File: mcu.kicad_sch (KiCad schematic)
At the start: 30 parts, among them J1 SM03B-SRSS-TB, SW1 SW_Push, SW2 SW_Push, U1 RP2350_60QFN, U2 W25Q128JVS, Y1 ABM8-272-T3

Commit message: minor cleanup
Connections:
- net GND: no longer J1.MP (MountPin)
- no-connect marks 8 -> 9
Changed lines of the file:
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@@
-	)
-	(junction
-		(at 242.57 138.43)
-		(diameter 0)
-		(color 0 0 0 0)
 	)
 	(junction
@@
 	)
 	(no_connect
+		(at 248.92 137.16)
+	)
+	(no_connect
 		(at 175.26 147.32)
 	)
@@
 	(wire
 		(pts
-			(xy 242.57 138.43) (xy 242.57 140.97)
+			(xy 242.57 129.54) (xy 242.57 140.97)
 		)
 		(stroke
@@
 	(wire
 		(pts
-			(xy 242.57 138.43) (xy 248.92 138.43)
-		)
-		(stroke
-			(width 0)
-			(type default)
-		)
-	)
-	(wire
-		(pts
 			(xy 175.26 68.58) (xy 185.42 68.58)
 		)
@@
 	(wire
 		(pts
-			(xy 242.57 129.54) (xy 242.57 138.43)
-		)
-		(stroke
-			(width 0)
-			(type default)
-		)
-	)
-	(wire
-		(pts
 			(xy 201.93 41.91) (xy 190.5 41.91)
 		)
@@
 		)
 		(stroke
-			(width 0)
-			(type default)
-		)
-	)
-	(wire
-		(pts
-			(xy 248.92 137.16) (xy 248.92 138.43)
-		)
-		(stroke

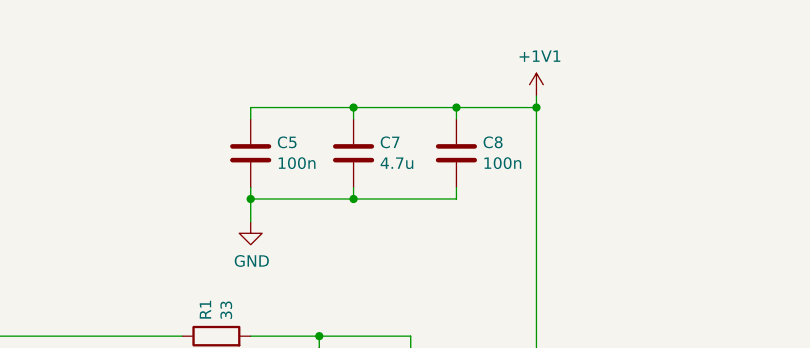
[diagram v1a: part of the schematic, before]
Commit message: add silkscreen, optimize layout and replace sd card peripheral
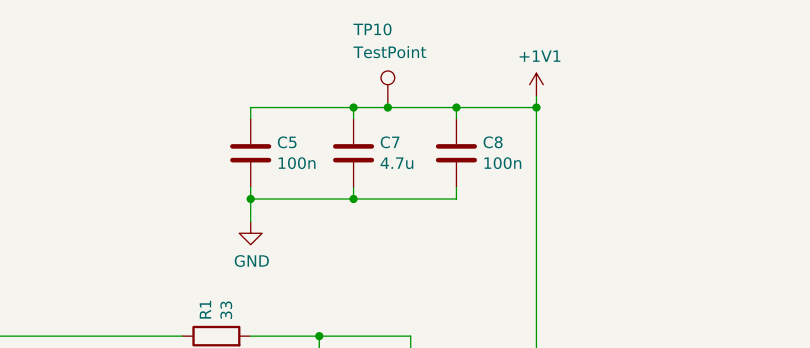
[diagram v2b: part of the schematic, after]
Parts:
- added TP10: TestPoint, TestPoint:TestPoint_Pad_D1.0mm, symbol Connector:TestPoint
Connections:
- net +1V1: now also TP10.1
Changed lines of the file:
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@@
+	)
+	(junction
+		(at 104.14 30.48)
+		(diameter 0)
+		(color 0 0 0 0)
 	)
 	(junction
@@
 	(wire
 		(pts
+			(xy 104.14 30.48) (xy 111.76 30.48)
+		)
+		(stroke
+			(width 0)
+			(type default)
+		)
+	)
+	(wire
+		(pts
 			(xy 62.23 82.55) (xy 111.76 82.55)
 		)
@@
 	(wire
 		(pts
-			(xy 100.33 30.48) (xy 111.76 30.48)
+			(xy 100.33 30.48) (xy 104.14 30.48)
 		)
 		(stroke
@@
 					(unit 1)
 				)
+			)
+		)
+	)
+	(symbol
+		(lib_id "Connector:TestPoint")
+		(at 104.14 30.48 0)
+		(unit 1)
+		(exclude_from_sim no)
+		(in_bom yes)
+		(on_board yes)
+		(dnp no)
+		(property "Reference" "TP10"
+			(at 100.33 21.844 0)
+			(effects
+				(font
+					(size 1.27 1.27)
+				)
+				(justify left)
+			)
+		)
+		(property "Value" "TestPoint"
+			(at 100.33 24.384 0)
+			(effects
+				(font
+					(size 1.27 1.27)
+				)
+				(justify left)
+			)
+		)
+		(property "Footprint" "TestPoint:TestPoint_Pad_D1.0mm"
+			(at 109.22 30.48 0)
+			(effects
+				(font
+					(size 1.27 1.27)
+				)
+				(hide yes)
+			)
+		)
+		(property "Datasheet" "~"
+			(at 109.22 30.48 0)
+			(effects
+				(font
+					(size 1.27 1.27)
+				)
+				(hide yes)
+			)
+		)
+		(property "Description" "test point"
+			(at 104.14 30.48 0)
+			(effects
+				(font
+					(size 1.27 1.27)
+				)
+				(hide yes)
+			)
+		)
+		(property "LCSC" ""
+			(at 104.14 30.48 0)
+			(effects
+				(font
+					(size 1.27 1.27)
+				)
+				(hide yes)
+			)
+		)
+		(property "Manufacturer" ""
+			(at 104.14 30.48 0)
+			(effects
+				(font
+					(size 1.27 1.27)
+				)
+				(hide yes)
+			)
+		)
+		(property "Manufacturer Part Number" ""
+			(at 104.14 30.48 0)
+			(effects
+				(font
+					(size 1.27 1.27)
+				)
+				(hide yes)
+			)
+		)
+		(pin "1"
+		)
+		(instances
+			(project "gameboy"
+				(path "/f4643692-c319-40a7-82a2-3e775c0a417f/0c43a605-cda2-4793-9a29-301f6419db25"
+					(reference "TP10")
+					(unit 1)
+				)

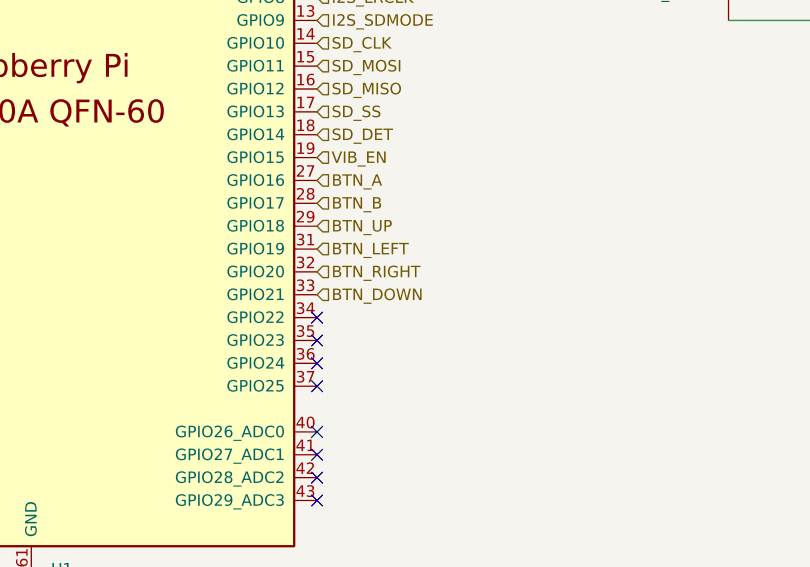
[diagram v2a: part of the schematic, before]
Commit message: add power monitoring
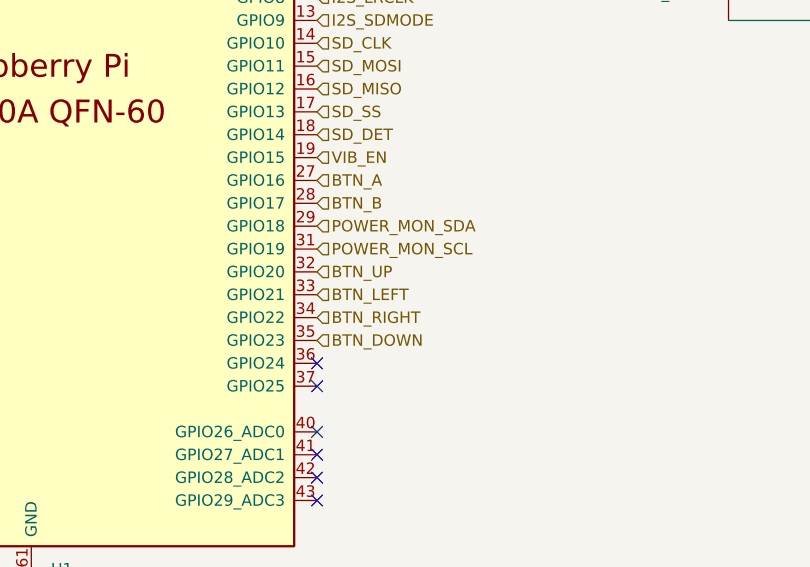
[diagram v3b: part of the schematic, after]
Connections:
- net BTN_DOWN: now also U1.35 (GPIO23); no longer U1.33 (GPIO21)
- net BTN_LEFT: now also U1.33 (GPIO21); no longer U1.31 (GPIO19)
- net BTN_RIGHT: now also U1.34 (GPIO22); no longer U1.32 (GPIO20)
- net BTN_UP: now also U1.32 (GPIO20); no longer U1.29 (GPIO18)
- new net POWER_MON_SCL: U1.31 (GPIO19)
- new net POWER_MON_SDA: U1.29 (GPIO18)
- no-connect marks 9 -> 7
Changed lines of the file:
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@@
-	)
-	(no_connect
-		(at 175.26 137.16)
 	)
 	(no_connect
@@
 	)
 	(no_connect
-		(at 175.26 134.62)
-	)
-	(no_connect
 		(at 248.92 137.16)
 	)
@@
 	(hierarchical_label "BTN_UP"
 		(shape input)
+		(at 175.26 129.54 0)
+		(effects
+			(font
+				(size 1.27 1.27)
+			)
+			(justify left)
+		)
+	)
+	(hierarchical_label "SD_MISO"
+		(shape input)
+		(at 175.26 109.22 0)
+		(effects
+			(font
+				(size 1.27 1.27)
+			)
+			(justify left)
+		)
+	)
+	(hierarchical_label "SD_MOSI"
+		(shape input)
+		(at 175.26 106.68 0)
+		(effects
+			(font
+				(size 1.27 1.27)
+			)
+			(justify left)
+		)
+	)
+	(hierarchical_label "POWER_MON_SDA"
+		(shape input)
 		(at 175.26 124.46 0)
 		(effects
@@
 		)
 	)
-	(hierarchical_label "SD_MISO"
-		(shape input)
-		(at 175.26 109.22 0)
-		(effects
-			(font
-				(size 1.27 1.27)
-			)
-			(justify left)
-		)
-	)
-	(hierarchical_label "SD_MOSI"
-		(shape input)
-		(at 175.26 106.68 0)
-		(effects
-			(font
-				(size 1.27 1.27)
-			)
-			(justify left)
-		)
-	)
 	(hierarchical_label "LCD_DC"
 		(shape input)
@@
 		)
 	)
+	(hierarchical_label "POWER_MON_SCL"
+		(shape input)
+		(at 175.26 127 0)
+		(effects
+			(font
+				(size 1.27 1.27)
+			)
+			(justify left)
+		)
+	)
 	(hierarchical_label "I2S_DIN"
 		(shape input)
@@
 	(hierarchical_label "BTN_RIGHT"
 		(shape input)
-		(at 175.26 129.54 0)
+		(at 175.26 134.62 0)
 		(effects
 			(font
@@
 	(hierarchical_label "BTN_LEFT"
 		(shape input)
-		(at 175.26 127 0)
+		(at 175.26 132.08 0)
 		(effects
 			(font
@@
 	(hierarchical_label "BTN_DOWN"
 		(shape input)
-		(at 175.26 132.08 0)
-		(effects
-			(font
+		(at 175.26 137.16 0)
+		(effects
+			(font

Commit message: changes for production
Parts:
- R2, R3, R6: footprint Resistor_SMD:R_0402_1005Metric -> Resistor_SMD:R_0603_1608Metric
- SW1, SW2: LCSC (none) -> C5504987; Manufacturer (none) -> Wurth Elektronik; Manufacturer Part Number (none) -> 434133025816
- TP10: now left out of the parts list
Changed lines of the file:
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@@
 			)
 		)
+		(property "LCSC" "C5504987"
+			(at 100.33 132.08 0)
+			(effects
+				(font
+					(size 1.27 1.27)
+				)
+				(hide yes)
+			)
+		)
+		(property "Manufacturer" "Wurth Elektronik"
+			(at 100.33 132.08 0)
+			(effects
+				(font
+					(size 1.27 1.27)
+				)
+				(hide yes)
+			)
+		)
+		(property "Manufacturer Part Number" "434133025816"
+			(at 100.33 132.08 0)
+			(effects
+				(font
+					(size 1.27 1.27)
+				)
+				(hide yes)
+			)
+		)
 		(pin "1"
 		)
@@
 	)
 	(symbol
+		(lib_id "Switch:SW_Push")
+		(at 220.98 96.52 90)
+		(unit 1)
+		(exclude_from_sim no)
+		(in_bom yes)
+		(on_board yes)
+		(dnp no)
+		(property "Reference" "SW2"
+			(at 215.138 96.52 0)
+			(effects
+				(font
+					(size 1.27 1.27)
+				)
+			)
+		)
+		(property "Value" "SW_Push"
+			(at 216.8961 96.52 0)
+			(effects
+				(font
+					(size 1.27 1.27)
+				)
+			)
+		)
+		(property "Footprint" "Button_Switch_SMD:SW_Push_1P1T_NO_Vertical_Wuerth_434133025816"
+			(at 215.9 96.52 0)
+			(effects
+				(font
+					(size 1.27 1.27)
+				)
+				(hide yes)
+			)
+		)
+		(property "Datasheet" "~"
+			(at 215.9 96.52 0)
+			(effects
+				(font
+					(size 1.27 1.27)
+				)
+				(hide yes)
+			)
+		)
+		(property "Description" ""
+			(at 220.98 96.52 0)
+			(effects
+				(font
+					(size 1.27 1.27)
+				)
+			)
+		)
+		(property "LCSC" "C5504987"
+			(at 220.98 96.52 0)
+			(effects
+				(font
+					(size 1.27 1.27)
+				)
+				(hide yes)
+			)
+		)
+		(property "Manufacturer" "Wurth Elektronik"
+			(at 220.98 96.52 0)
+			(effects
+				(font
+					(size 1.27 1.27)
+				)
+				(hide yes)
+			)
+		)
+		(property "Manufacturer Part Number" "434133025816"
+			(at 220.98 96.52 0)
+			(effects
+				(font
+					(size 1.27 1.27)
+				)
+				(hide yes)
+			)
+		)
+		(pin "1"
+		)
+		(pin "2"
+		)
+		(instances
+			(project "gameboy"
+				(path "/f4643692-c319-40a7-82a2-3e775c0a417f/0c43a605-cda2-4793-9a29-301f6419db25"
+					(reference "SW2")
+					(unit 1)
+				)
+			)
+		)
+	)
+	(symbol
 		(lib_id "Device:R")
 		(at 220.98 85.09 0)
@@
 			)
 		)
-		(property "Footprint" "Resistor_SMD:R_0402_1005Metric"
+		(property "Footprint" "Resistor_SMD:R_0603_1608Metric"
 			(at 219.202 85.09 90)
 			(effects
@@
 			)
 		)
+		(property "LCSC" ""
+			(at 220.98 85.09 0)
+			(effects
+				(font
+					(size 1.27 1.27)
+				)
+				(hide yes)
+			)
+		)
+		(property "Manufacturer" ""
+			(at 220.98 85.09 0)
+			(effects
+				(font
+					(size 1.27 1.27)
+				)
+				(hide yes)
+			)
+		)
+		(property "Manufacturer Part Number" ""
+			(at 220.98 85.09 0)
+			(effects
+				(font
+					(size 1.27 1.27)
+				)
+				(hide yes)
+			)
+		)
 		(pin "1"
 		)
@@
 		(unit 1)
 		(exclude_from_sim no)
-		(in_bom yes)
+		(in_bom no)
 		(on_board yes)
 		(dnp no)
@@
 			)
 		)
-		(property "Footprint" "Resistor_SMD:R_0402_1005Metric"
+		(property "Footprint" "Resistor_SMD:R_0603_1608Metric"
 			(at 86.36 120.142 90)
 			(effects
@@
 			)
 		)
+		(property "LCSC" ""
+			(at 86.36 121.92 0)
+			(effects
+				(font
+					(size 1.27 1.27)
+				)
+				(hide yes)
+			)
+		)
+		(property "Manufacturer" ""
+			(at 86.36 121.92 0)
+			(effects
+				(font
+					(size 1.27 1.27)
+				)
+				(hide yes)
+			)
+		)
+		(property "Manufacturer Part Number" ""
+			(at 86.36 121.92 0)
+			(effects
+				(font
+					(size 1.27 1.27)
+				)
+				(hide yes)
+			)
+		)
 		(pin "1"
 		)
@@
 			)
 		)
-		(property "Footprint" "Resistor_SMD:R_0402_1005Metric"
+		(property "Footprint" "Resistor_SMD:R_0603_1608Metric"
 			(at 87.63 130.302 90)
 			(effects
@@
 			)
 		)
-		(pin "1"
-		)
-		(pin "2"
-		)
-		(instances
-			(project "gameboy"
-				(path "/f4643692-c319-40a7-82a2-3e775c0a417f/0c43a605-cda2-4793-9a29-301f6419db25"
-					(reference "R3")
-					(unit 1)
-				)
-			)
-		)
-	)
-	(symbol
-		(lib_id "power:+1V1")
-		(at 62.23 67.31 0)
-		(unit 1)
-		(exclude_from_sim no)
-		(in_bom yes)
-		(on_board yes)
-		(dnp no)
-		(property "Reference" "#PWR04"
-			(at 62.23 71.12 0)
+		(property "LCSC" ""
+			(at 87.63 132.08 0)
 			(effects
 				(font
@@
 			)
 		)
-		(property "Value" "+1V1"
-			(at 62.611 62.9158 0)
-			(effects
-				(font
-					(size 1.27 1.27)
-				)
-			)
-		)
-		(property "Footprint" ""
-			(at 62.23 67.31 0)
+		(property "Manufacturer" ""
+			(at 87.63 132.08 0)
 			(effects
 				(font
@@
 			)
 		)
-		(property "Datasheet" ""
-			(at 62.23 67.31 0)
+		(property "Manufacturer Part Number" ""
+			(at 87.63 132.08 0)
 			(effects
 				(font
@@
 			)
 		)
-		(property "Description" ""
-			(at 62.23 67.31 0)
-			(effects
-				(font
-					(size 1.27 1.27)
-				)
-			)
-		)
 		(pin "1"
 		)
+		(pin "2"
+		)
 		(instances
 			(project "gameboy"
 				(path "/f4643692-c319-40a7-82a2-3e775c0a417f/0c43a605-cda2-4793-9a29-301f6419db25"
-					(reference "#PWR04")
+					(reference "R3")
 					(unit 1)
 				)
@@
 	)
 	(symbol
-		(lib_id "Switch:SW_Push")
-		(at 220.98 96.52 90)
+		(lib_id "power:+1V1")
+		(at 62.23 67.31 0)
 		(unit 1)
 		(exclude_from_sim no)
@@
 		(on_board yes)
 		(dnp no)
-		(property "Reference" "SW2"
-			(at 214.63 96.52 90)
+		(property "Reference" "#PWR04"
+			(at 62.23 71.12 0)
 			(effects
 				(font
 					(size 1.27 1.27)
 				)
+				(hide yes)
 			)
 		)
-		(property "Value" "SW_Push"
-			(at 214.63 98.552 90)
+		(property "Value" "+1V1"
+			(at 62.611 62.9158 0)
 			(effects
 				(font
@@
 			)
 		)
-		(property "Footprint" "Button_Switch_SMD:SW_Push_1P1T_NO_Vertical_Wuerth_434133025816"
-			(at 215.9 96.52 0)
+		(property "Footprint" ""
+			(at 62.23 67.31 0)
 			(effects
 				(font
@@
 			)
 		)
-		(property "Datasheet" "~"
-			(at 215.9 96.52 0)
+		(property "Datasheet" ""
+			(at 62.23 67.31 0)
 			(effects
 				(font
@@
 		)
 		(property "Description" ""
-			(at 220.98 96.52 0)
+			(at 62.23 67.31 0)
 			(effects
 				(font
@@
 		(pin "1"
 		)
-		(pin "2"
-		)
 		(instances
 			(project "gameboy"
 				(path "/f4643692-c319-40a7-82a2-3e775c0a417f/0c43a605-cda2-4793-9a29-301f6419db25"
-					(reference "SW2")
+					(reference "#PWR04")
 					(unit 1)
 				)

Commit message: fix bom
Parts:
- C1, C4: value 4.7u -> 4.7uF; footprint RP2350_60QFN_minimal:C_0402_1005Metric_small_pads -> Capacitor_SMD:C_0402_1005Metric
- C10, C11, C12, C13, C14, C15, C16, C31, C5, C8, C9: value 100n -> 100nF
- C2, C3: value 15p -> 15pF
- C6, C7: value 4.7u -> 4.7uF
- J1: LCSC (none) -> C160403
- R1: value 33 -> 33R
- R4, R5: value 27 -> 27R
- SW1, SW2: LCSC C5504987 -> C843674
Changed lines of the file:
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@@
 			)
 		)
-		(property "Value" "100n"
+		(property "Value" "100nF"
 			(at 256.921 67.183 0)
 			(effects
@@
 			)
 		)
-		(property "LCSC" "C5504987"
+		(property "LCSC" "C843674"
 			(at 100.33 132.08 0)
 			(effects
@@
 			)
 		)
-		(property "Value" "4.7u"
+		(property "Value" "4.7uF"
 			(at 103.251 36.703 0)
 			(effects
@@
 			)
 		)
-		(property "Value" "100n"
+		(property "Value" "100nF"
 			(at 239.141 36.703 0)
 			(effects
@@
 			)
 		)
-		(property "LCSC" "C5504987"
+		(property "LCSC" "C843674"
 			(at 220.98 96.52 0)
 			(effects
@@
 			)
 		)
-		(property "Value" "100n"
+		(property "Value" "100nF"
 			(at 250.571 36.703 0)
 			(effects
@@
 			)
 		)
-		(property "Value" "100n"
+		(property "Value" "100nF"
 			(at 227.711 36.703 0)
 			(effects
@@
 			)
 		)
-		(property "Value" "100n"
+		(property "Value" "100nF"
 			(at 170.561 36.703 0)
 			(effects
@@
 			)
 		)
-		(property "Value" "4.7u"
+		(property "Value" "4.7uF"
 			(at 100.33 62.23 0)
 			(effects
@@
 			)
 		)
-		(property "Value" "15p"
+		(property "Value" "15pF"
 			(at 52.197 124.841 0)
 			(effects
@@
 			)
 		)
-		(property "Value" "4.7u"
+		(property "Value" "4.7uF"
 			(at 66.04 74.93 0)
 			(effects
@@
 			)
 		)
-		(property "Footprint" "RP2350_60QFN_minimal:C_0402_1005Metric_small_pads"
+		(property "Footprint" "Capacitor_SMD:C_0402_1005Metric"
 			(at 63.1952 77.47 0)
 			(effects
@@
 			)
 		)
-		(property "LCSC" ""
+		(property "LCSC" "C160403"
 			(at 248.92 129.54 0)
 			(effects
@@
 			)
 		)
-		(property "Value" "100n"
+		(property "Value" "100nF"
 			(at 181.991 36.703 0)
 			(effects
@@
 			)
 		)
-		(property "Value" "100n"
+		(property "Value" "100nF"
 			(at 114.681 36.703 0)
 			(effects
@@
 			)
 		)
-		(property "Value" "100n"
+		(property "Value" "100nF"
 			(at 91.821 36.703 0)
 			(effects
@@
 			)
 		)
-		(property "Value" "15p"
+		(property "Value" "15pF"
 			(at 52.197 114.681 0)
 			(effects
@@
 			)
 		)
-		(property "Value" "33"
+		(property "Value" "33R"
 			(at 86.233 54.102 0)
 			(effects
@@
 			)
 		)
-		(property "Value" "27"
+		(property "Value" "27R"
 			(at 189.23 76.2 90)
 			(effects
@@
 			)
 		)
-		(property "Value" "100n"
+		(property "Value" "100nF"
 			(at 193.421 36.703 0)
 			(effects
@@
 			)
 		)
-		(property "Value" "4.7u"
+		(property "Value" "4.7uF"
 			(at 53.721 75.3622 0)
 			(effects
@@
 			)
 		)
-		(property "Footprint" "RP2350_60QFN_minimal:C_0402_1005Metric_small_pads"
+		(property "Footprint" "Capacitor_SMD:C_0402_1005Metric"
 			(at 51.7652 77.47 0)
 			(effects
@@
 			)
 		)
-		(property "Value" "100n"
+		(property "Value" "100nF"
 			(at 204.851 36.703 0)
 			(effects
@@
 			)
 		)
-		(property "Value" "100n"
+		(property "Value" "100nF"
 			(at 216.281 36.703 0)
 			(effects
@@
 			)
 		)
-		(property "Value" "27"
+		(property "Value" "27R"
 			(at 189.23 65.6336 90)
 			(effects

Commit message: use one lower mlq component
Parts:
- U2: LCSC C97521 -> C113767
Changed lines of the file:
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@@
 			)
 		)
-		(property "LCSC" "C97521"
+		(property "LCSC" "C113767"
 			(at 247.65 81.28 0)
 			(effects

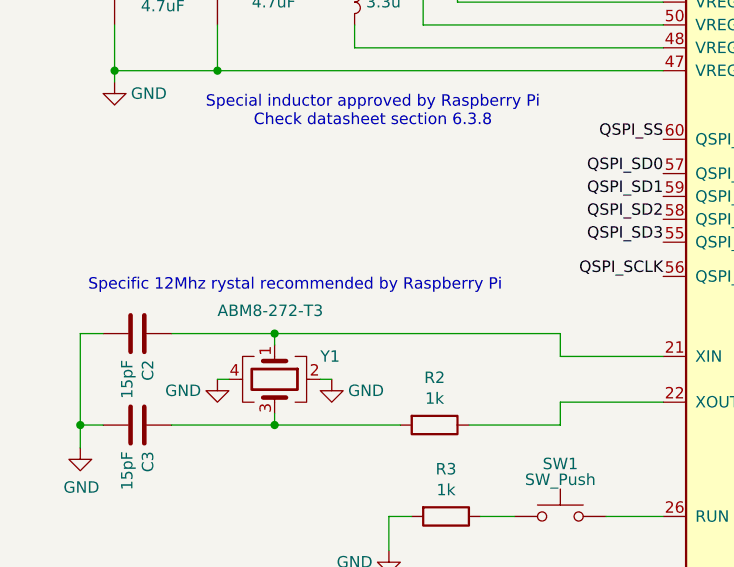
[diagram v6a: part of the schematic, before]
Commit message: add fiducials and mounting holes
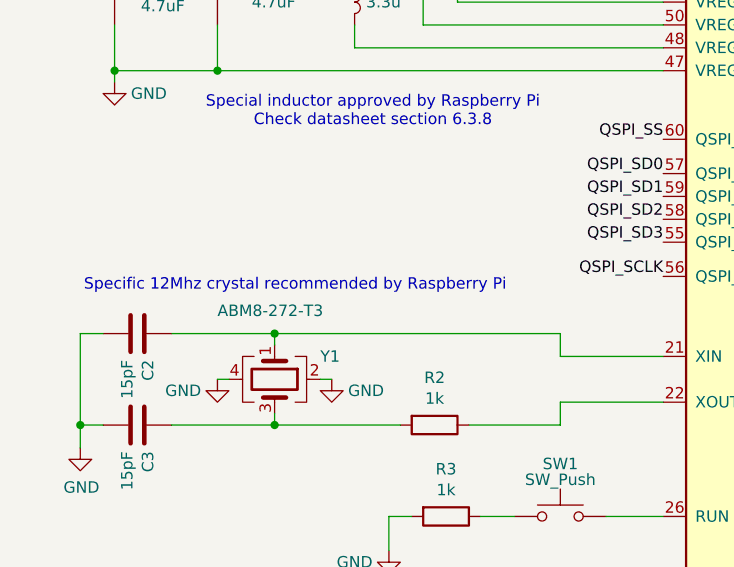
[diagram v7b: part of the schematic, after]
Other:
- note added: "Specific 12Mhz crystal recommended by Raspberry Pi"
- note removed: "Specific 12Mhz rystal recommended by Raspberry Pi"
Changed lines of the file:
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@@
 		)
 	)
-	(text "Specific 12Mhz rystal recommended by Raspberry Pi"
+	(text "Specific 12Mhz crystal recommended by Raspberry Pi"
 		(exclude_from_sim no)
 		(at 70.866 106.426 0)
